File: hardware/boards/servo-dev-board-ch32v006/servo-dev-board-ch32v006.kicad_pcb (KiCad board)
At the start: 4 copper layers, 60 x 60 mm, 88 parts, among them J1 JST-PH-H, J2 TERM, J3 PIN-V, J4 JST-ZH-H, J5 PIN-V, J6 PIN-V, J7 PIN-V, J8 PIN-V, J9 JST-PH-V, SW1 SW_Push, U1 HT7533-1, U2 DRV8212PDSGR, U3 CH32V006F8P6, U4 74LVC2G241

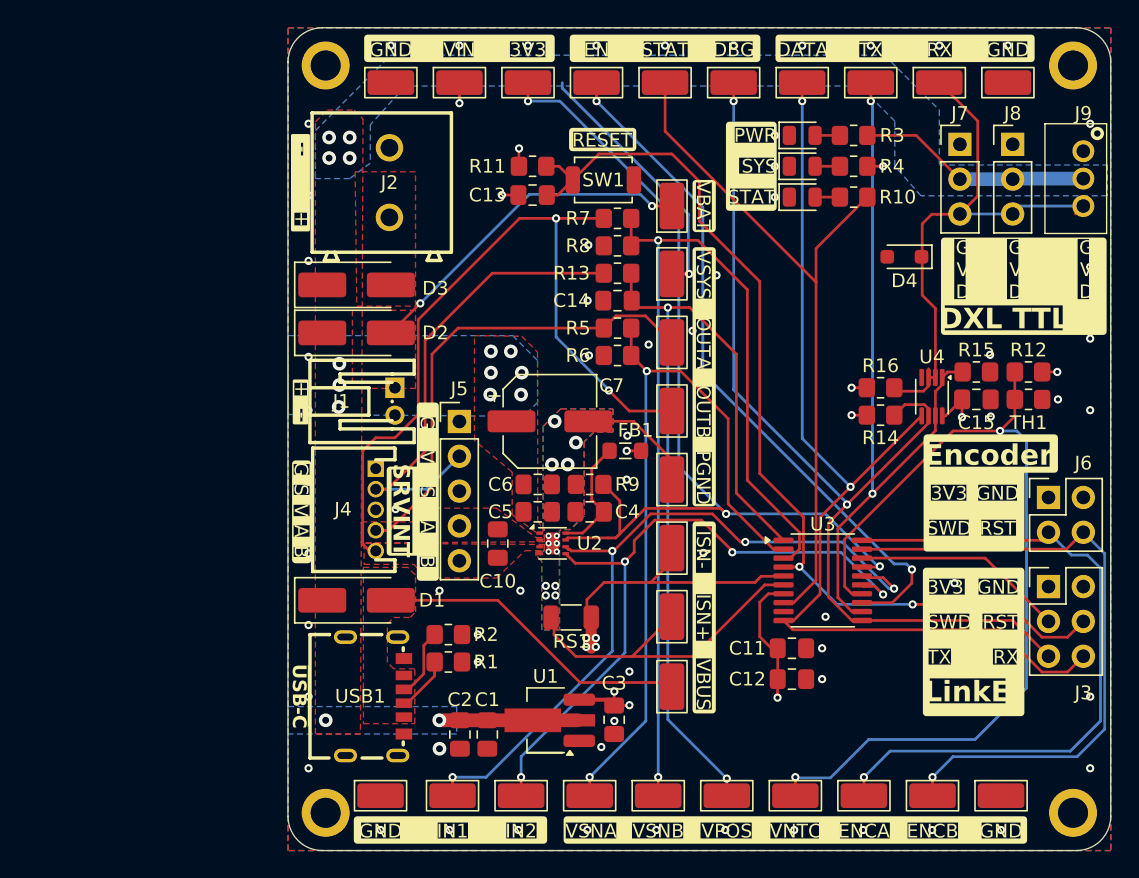
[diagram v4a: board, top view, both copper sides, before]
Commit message: fix LDO output caps
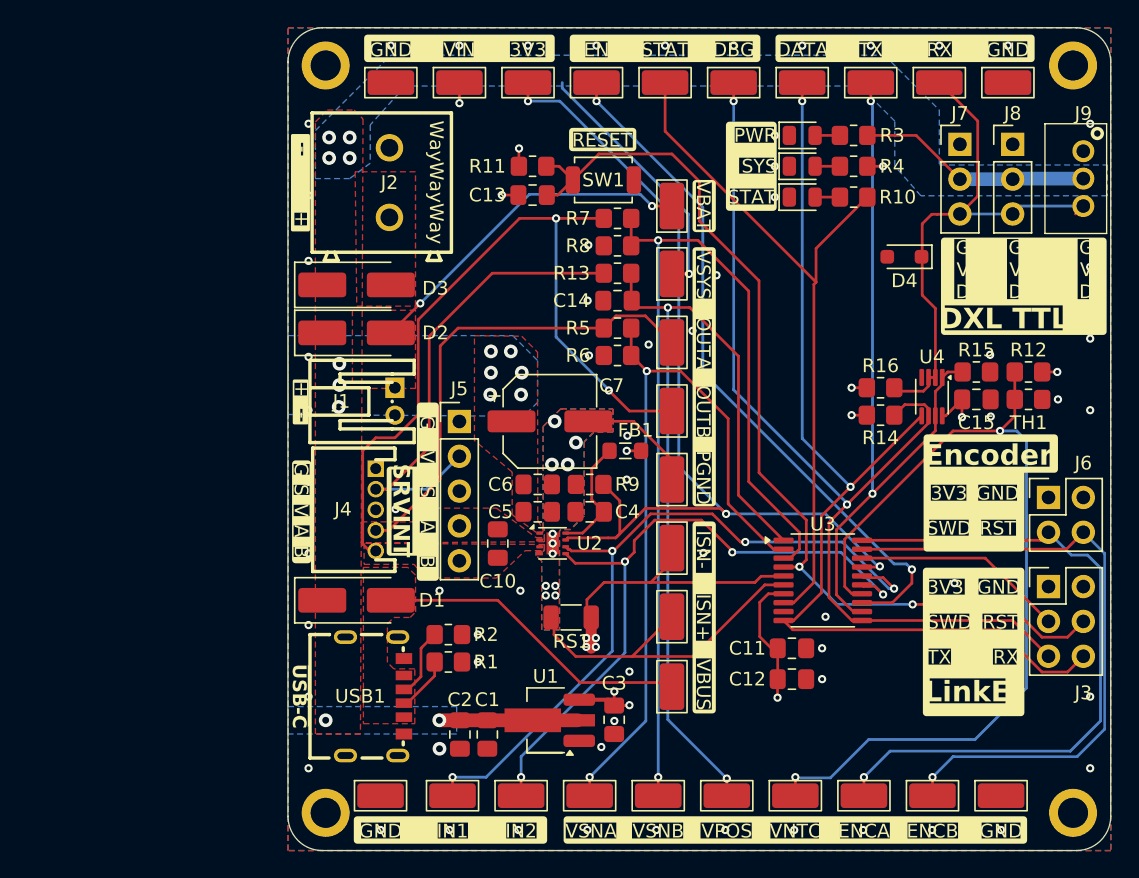
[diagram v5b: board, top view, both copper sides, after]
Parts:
- C3: value 1µF -> 10µF
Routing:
- net /DATA: track 40.5 -> 39.9 mm
- net PGND: vias 14 -> 11
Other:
- board text added: "WayWayWay"

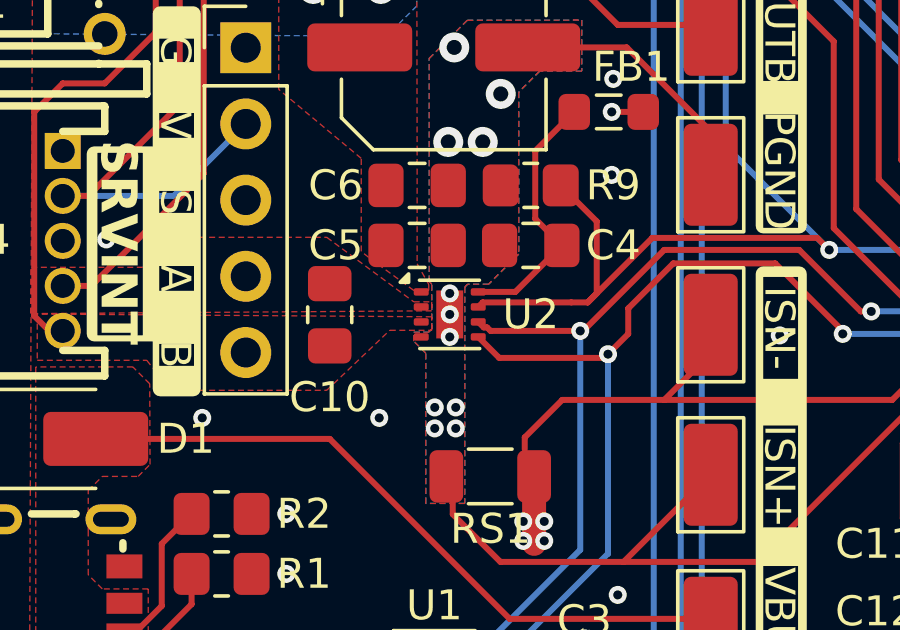
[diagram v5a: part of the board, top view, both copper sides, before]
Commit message: better thermal under DRV using staggered 2x3 0.3mm vias
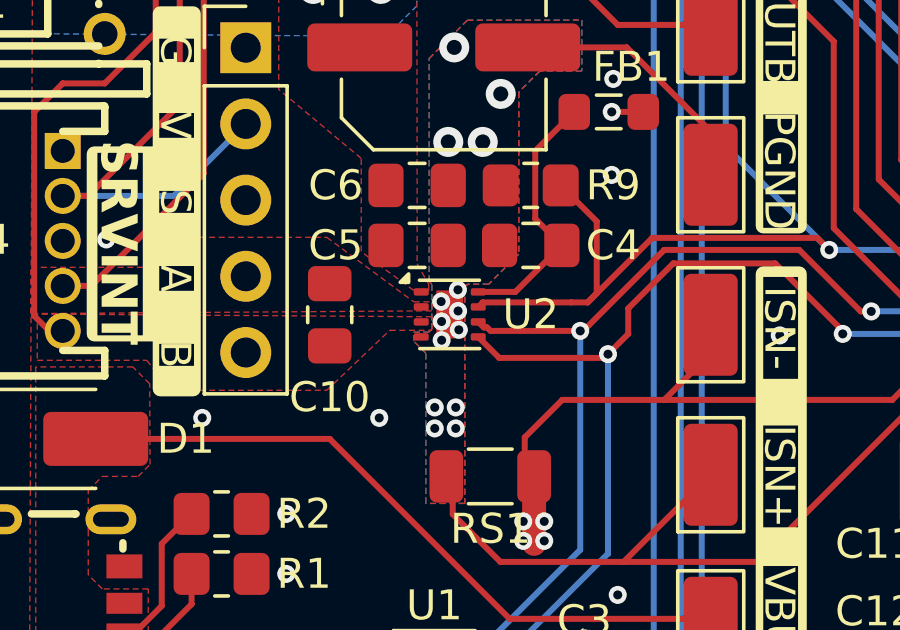
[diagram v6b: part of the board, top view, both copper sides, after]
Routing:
- net PGND: vias 11 -> 14
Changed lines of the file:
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@@
 	)
 	(via
-		(at 149.3 91.9)
+		(at 149.573004 91.779366)
 		(size 0.6)
 		(drill 0.3)
@@
 	)
 	(via
-		(at 149.3 93.35)
+		(at 149.578253 92.485418)
 		(size 0.6)
 		(drill 0.3)
@@
 		(layers "F.Cu" "B.Cu")
 		(free yes)
+		(net 4)
+	)
+	(via
+		(at 149.027 92.836522)
+		(size 0.6)
+		(drill 0.3)
+		(layers "F.Cu" "B.Cu")
+		(net 4)
+	)
+	(via
+		(at 149.03 93.46)
+		(size 0.6)
+		(drill 0.3)
+		(layers "F.Cu" "B.Cu")
+		(net 4)
+	)
+	(via
+		(at 149.603738 93.113388)
+		(size 0.6)
+		(drill 0.3)
+		(layers "F.Cu" "B.Cu")
 		(net 4)
 	)
@@
 	)
 	(via
-		(at 149.3 92.6)
+		(at 149.013398 92.171354)
 		(size 0.6)
 		(drill 0.3)

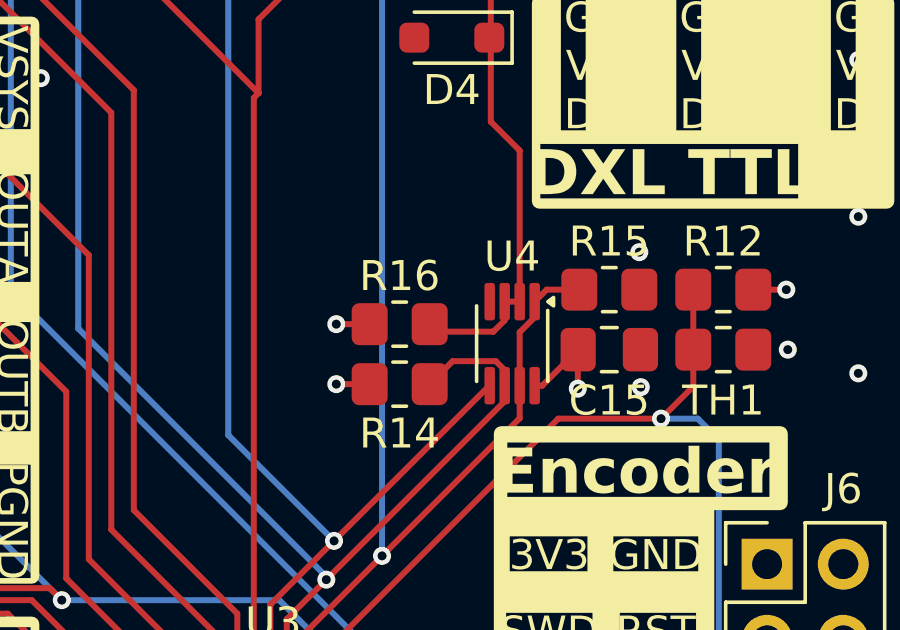
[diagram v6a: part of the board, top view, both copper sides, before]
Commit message: fix 74LVC2G241 footprint. Pin clearance was 0.15mm. PCBWay minimum is 0.2mm. Corrent Pin width is 0.3mm with pitch of 0.5mm, leaving 0.2mm clearance. Standard KiCad Library's pin width was 0.35mm, leaving only 0.15mm of clearance, which PCBWay rejected for their standard process.
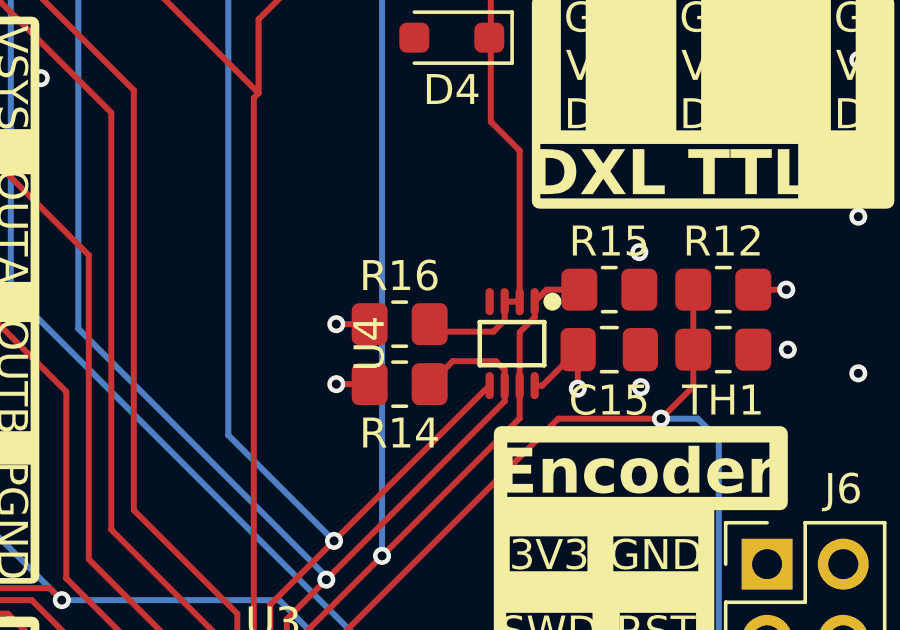
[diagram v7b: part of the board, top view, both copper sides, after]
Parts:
- U4: footprint Package_SO:VSSOP-8_2.3x2mm_P0.5mm -> shared:VSSOP-8_L2.3-W2.0-P0.50-LS3.1-BR
- turned U4 to 90 degrees
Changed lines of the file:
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@@
 		)
 	)
-	(footprint "Package_SO:VSSOP-8_2.3x2mm_P0.5mm"
+	(footprint "shared:VSSOP-8_L2.3-W2.0-P0.50-LS3.1-BR"
 		(layer "F.Cu")
-		(at 176.9625 81.9 -90)
-		(descr "VSSOP, 8 Pin (https://www.jedec.org/standards-documents/docs/mo-187-f), generated with kicad-footprint-generator ipc_gullwing_generator.py")
-		(tags "VSSOP SO JEDEC-MO-187-CA Texas_DCU0008A")
+		(at 176.9625 81.9 90)
 		(property "Reference" "U4"
-			(at -2.9 0 180)
+			(at 0 -4.75 90)
 			(layer "F.SilkS")
 			(effects
@@
 		)
 		(property "Value" "74LVC2G241"
-			(at 0 1.95 90)
-			(layer "F.Fab")
-			(hide yes)
+			(at 0 4.75 90)
+			(layer "F.Fab")
 			(effects
 				(font
@@
 		)
 		(property "LCSC" "C10430"
-			(at 0 0 270)
+			(at 0 0 90)
 			(unlocked yes)
 			(layer "F.Fab")
@@
 		)
 		(property "JLC Type" "Extended"
-			(at 0 0 270)
+			(at 0 0 90)
 			(unlocked yes)
 			(layer "F.Fab")
@@
 		(attr smd)
 		(fp_line
-			(start 1.26 1.185)
-			(end -1.26 1.185)
-			(stroke
-				(width 0.12)
-				(type solid)
-			)
-			(layer "F.SilkS")
-		)
-		(fp_line
-			(start -1.105568 -1.185)
-			(end 1.26 -1.185)
-			(stroke
-				(width 0.12)
-				(type solid)
-			)
-			(layer "F.SilkS")
-		)
-		(fp_poly
-			(pts
-				(xy -1.4 -1.19) (xy -1.54 -1.38) (xy -1.26 -1.38)
-			)
-			(stroke
-				(width 0.12)
-				(type solid)
-			)
-			(fill yes)
-			(layer "F.SilkS")
-		)
-		(fp_line
-			(start -1.4 1.25)
-			(end -1.4 1.18)
-			(stroke
-				(width 0.05)
-				(type solid)
-			)
-			(layer "F.CrtYd")
-		)
-		(fp_line
-			(start 1.4 1.25)
-			(end -1.4 1.25)
-			(stroke
-				(width 0.05)
-				(type solid)
-			)
-			(layer "F.CrtYd")
-		)
-		(fp_line
-			(start -2.28 1.18)
-			(end -2.28 -1.18)
-			(stroke
-				(width 0.05)
-				(type solid)
-			)
-			(layer "F.CrtYd")
-		)
-		(fp_line
-			(start -1.4 1.18)
-			(end -2.28 1.18)
-			(stroke
-				(width 0.05)
-				(type solid)
-			)
-			(layer "F.CrtYd")
-		)
-		(fp_line
-			(start 1.4 1.18)
-			(end 1.4 1.25)
-			(stroke
-				(width 0.05)
-				(type solid)
-			)
-			(layer "F.CrtYd")
-		)
-		(fp_line
-			(start 2.28 1.18)
-			(end 1.4 1.18)
-			(stroke
-				(width 0.05)
-				(type solid)
-			)
-			(layer "F.CrtYd")
-		)
-		(fp_line
-			(start -2.28 -1.18)
-			(end -1.4 -1.18)
-			(stroke
-				(width 0.05)
-				(type solid)
-			)
-			(layer "F.CrtYd")
-		)
-		(fp_line
-			(start -1.4 -1.18)
-			(end -1.4 -1.25)
-			(stroke
-				(width 0.05)
-				(type solid)
-			)
-			(layer "F.CrtYd")
-		)
-		(fp_line
-			(start 1.4 -1.18)
-			(end 2.28 -1.18)
-			(stroke
-				(width 0.05)
-				(type solid)
-			)
-			(layer "F.CrtYd")
-		)
-		(fp_line
-			(start 2.28 -1.18)
-			(end 2.28 1.18)
-			(stroke
-				(width 0.05)
-				(type solid)
-			)
-			(layer "F.CrtYd")
-		)
-		(fp_line
-			(start -1.4 -1.25)
-			(end 1.4 -1.25)
-			(stroke
-				(width 0.05)
-				(type solid)
-			)
-			(layer "F.CrtYd")
-		)
-		(fp_line
-			(start 1.4 -1.25)
-			(end 1.4 -1.18)
-			(stroke
-				(width 0.05)
-				(type solid)
-			)
-			(layer "F.CrtYd")
-		)
-		(fp_poly
-			(pts
-				(xy -0.65 -1) (xy 1.15 -1) (xy 1.15 1) (xy -1.15 1) (xy -1.15 -0.5)
-			)
-			(stroke
-				(width 0.1)
+			(start 0.72 -1.08)
+			(end 0.72 1.07)
+			(stroke
+				(width 0.15)
+				(type solid)
+			)
+			(layer "F.SilkS")
+		)
+		(fp_line
+			(start -0.72 -1.08)
+			(end 0.72 -1.08)
+			(stroke
+				(width 0.15)
+				(type solid)
+			)
+			(layer "F.SilkS")
+		)
+		(fp_line
+			(start 0.72 1.07)
+			(end -0.72 1.07)
+			(stroke
+				(width 0.15)
+				(type solid)
+			)
+			(layer "F.SilkS")
+		)
+		(fp_line
+			(start -0.72 1.07)
+			(end -0.72 -1.08)
+			(stroke
+				(width 0.15)
+				(type solid)
+			)
+			(layer "F.SilkS")
+		)
+		(fp_circle
+			(center 1.4 1.34)
+			(end 1.55 1.34)
+			(stroke
+				(width 0.3)
 				(type solid)
 			)
 			(fill no)
+			(layer "F.SilkS")
+		)
+		(fp_circle
+			(center 1.95 0.75)
+			(end 2.1 0.75)
+			(stroke
+				(width 0.3)
+				(type solid)
+			)
+			(fill no)
+			(layer "Cmts.User")
+		)
+		(fp_circle
+			(center 1.55 1)
+			(end 1.58 1)
+			(stroke
+				(width 0.06)
+				(type solid)
+			)
+			(fill no)
 			(layer "F.Fab")
 		)
@@
 			(effects
 				(font
-					(size 0.57 0.57)
-					(thickness 0.09)
-				)
-			)
-		)
-		(pad "1" smd roundrect
-			(at -1.4 -0.75 270)
-			(size 1.25 0.35)
-			(layers "F.Cu" "F.Mask" "F.Paste")
-			(roundrect_rratio 0.25)
+					(size 1 1)
+					(thickness 0.15)
+				)
+			)
+		)
+		(pad "1" smd oval
+			(at 1.4 0.75 180)
+			(size 0.28 0.91)
+			(layers "F.Cu" "F.Mask" "F.Paste")
 			(net 35 "/TX_EN")
 			(pintype "input")
 		)
-		(pad "2" smd roundrect
-			(at -1.4 -0.25 270)
-			(size 1.25 0.35)
-			(layers "F.Cu" "F.Mask" "F.Paste")
-			(roundrect_rratio 0.25)
+		(pad "2" smd oval
+			(at 1.4 0.25 180)
+			(size 0.28 0.91)
+			(layers "F.Cu" "F.Mask" "F.Paste")
 			(net 5 "/DATA")
 			(pintype "input")
 		)
-		(pad "3" smd roundrect
-			(at -1.4 0.25 270)
-			(size 1.25 0.35)
-			(layers "F.Cu" "F.Mask" "F.Paste")
-			(roundrect_rratio 0.25)
+		(pad "3" smd oval
+			(at 1.4 -0.25 180)
+			(size 0.28 0.91)
+			(layers "F.Cu" "F.Mask" "F.Paste")
 			(net 5 "/DATA")
 			(pintype "tri_state")
 		)
-		(pad "4" smd roundrect
-			(at -1.4 0.75 270)
-			(size 1.25 0.35)
-			(layers "F.Cu" "F.Mask" "F.Paste")
-			(roundrect_rratio 0.25)
+		(pad "4" smd oval
+			(at 1.4 -0.75 180)
+			(size 0.28 0.91)
+			(layers "F.Cu" "F.Mask" "F.Paste")
 			(net 1 "GND")
 			(pinfunction "GND")
 			(pintype "power_in")
 		)
-		(pad "5" smd roundrect
-			(at 1.4 0.75 270)
-			(size 1.25 0.35)
-			(layers "F.Cu" "F.Mask" "F.Paste")
-			(roundrect_rratio 0.25)
+		(pad "5" smd oval
+			(at -1.4 -0.75 180)
+			(size 0.28 0.91)
+			(layers "F.Cu" "F.Mask" "F.Paste")
 			(net 7 "/TX")
 			(pintype "input")
 		)
-		(pad "6" smd roundrect
-			(at 1.4 0.25 270)
-			(size 1.25 0.35)
-			(layers "F.Cu" "F.Mask" "F.Paste")
-			(roundrect_rratio 0.25)
+		(pad "6" smd oval
+			(at -1.4 -0.25 180)
+			(size 0.28 0.91)
+			(layers "F.Cu" "F.Mask" "F.Paste")
 			(net 13 "/RX")
 			(pintype "tri_state")
 		)
-		(pad "7" smd roundrect
-			(at 1.4 -0.25 270)
-			(size 1.25 0.35)
-			(layers "F.Cu" "F.Mask" "F.Paste")
-			(roundrect_rratio 0.25)
+		(pad "7" smd oval
+			(at -1.4 0.25 180)
+			(size 0.28 0.91)
+			(layers "F.Cu" "F.Mask" "F.Paste")
 			(net 35 "/TX_EN")
 			(pintype "input")
 		)
-		(pad "8" smd roundrect
-			(at 1.4 -0.75 270)
-			(size 1.25 0.35)
-			(layers "F.Cu" "F.Mask" "F.Paste")
-			(roundrect_rratio 0.25)
+		(pad "8" smd oval
+			(at -1.4 0.75 180)
+			(size 0.28 0.91)
+			(layers "F.Cu" "F.Mask" "F.Paste")
 			(net 23 "+3V3")
 			(pinfunction "VCC")
@@
 		)
 		(embedded_fonts no)
-		(model "${KICAD9_3DMODEL_DIR}/Package_SO.3dshapes/VSSOP-8_2.3x2mm_P0.5mm.step"
+		(model "${KIPRJMOD}/../../shared.3dshapes/VSSOP-8_L2.3-W2.0-P0.50-LS3.1-BL.wrl"
 			(offset
-				(xyz 0 0 0)
+				(xyz 0 -0 -0)
 			)
 			(scale
@@
 			)
 			(rotate
-				(xyz 0 0 0)
-			)
-		)
+				(xyz 0 0 270)
+			)
+		)
